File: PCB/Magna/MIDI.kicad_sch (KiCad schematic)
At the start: 14 parts, among them J1001 DIN-5_180degree, J1002 DIN-5_180degree, J1003 DIN-5_180degree, U1001 74HC08D, U1002 6N137

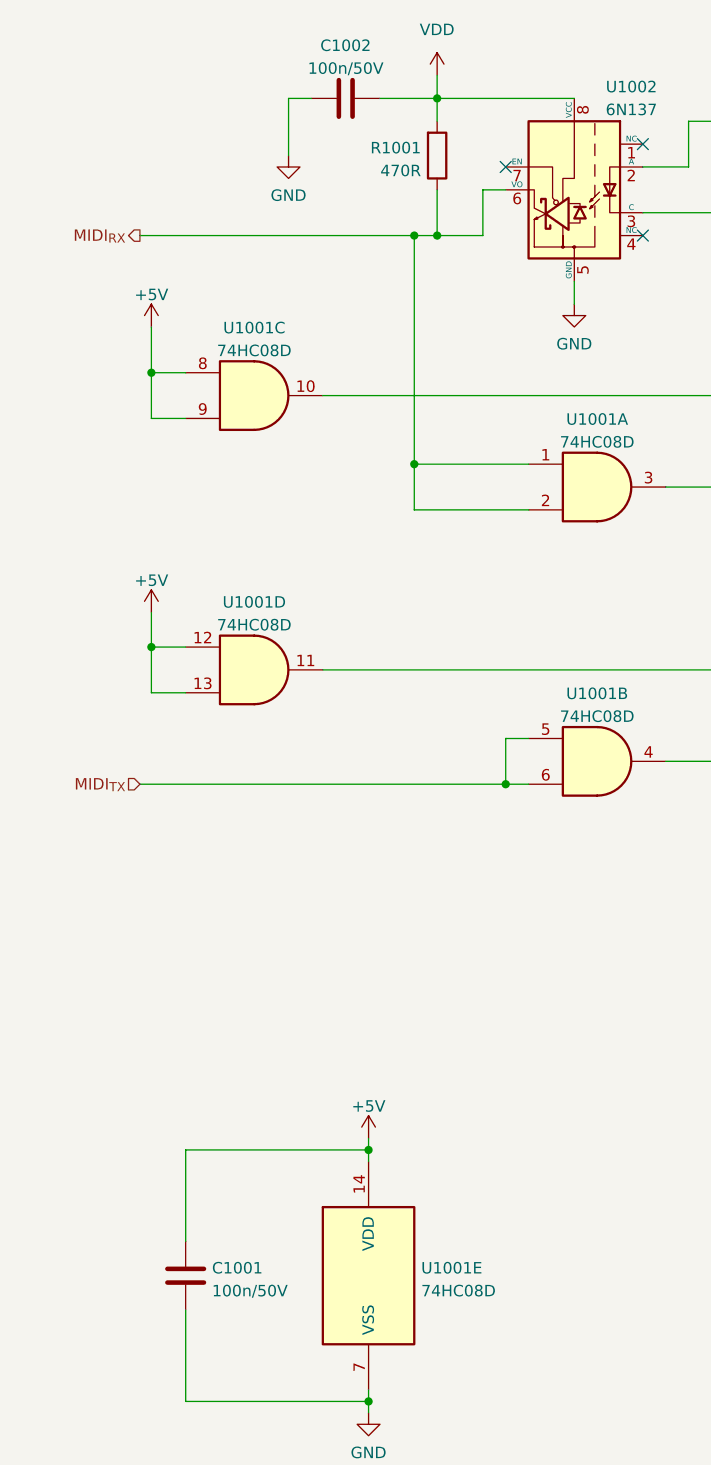
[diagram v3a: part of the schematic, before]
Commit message: Update capacitors to parts in JLC library
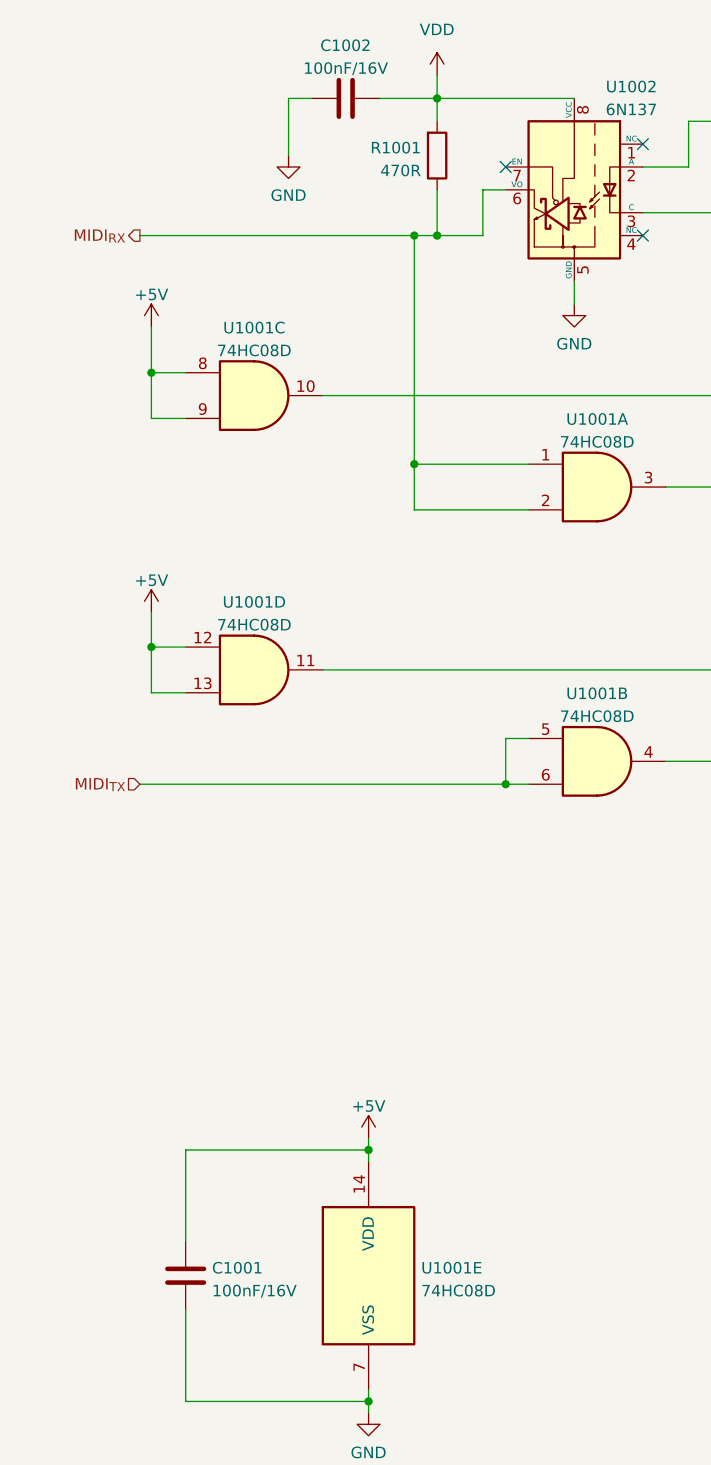
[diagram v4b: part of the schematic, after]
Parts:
- C1001, C1002: value 100n/50V -> 100nF/16V; footprint Capacitor_SMD:C_0603_1608Metric_Pad1.08x0.95mm_HandSolder -> Capacitor_SMD:C_0805_2012Metric; LCSC C14663 -> C218638
- D1001: LCSC C8598 -> (none)
- R1001: LCSC C23179 -> (none)
- R1002, R1003, R1004, R1005, R1006: LCSC C17557 -> (none)
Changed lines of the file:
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@@
       (effects (font (size 1.27 1.27)) hide)
     )
-    (property "LCSC" "C17557" (at 196.85 91.44 0)
+    (property "LCSC" "" (at 196.85 91.44 0)
       (effects (font (size 1.27 1.27)) hide)
     )
@@
       (effects (font (size 1.27 1.27)) (justify left))
     )
-    (property "Value" "100n/50V" (at 46.101 160.4522 0)
+    (property "Value" "100nF/16V" (at 46.101 160.4522 0)
       (effects (font (size 1.27 1.27)) (justify left))
     )
-    (property "Footprint" "Capacitor_SMD:C_0603_1608Metric_Pad1.08x0.95mm_HandSolder" (at 44.1452 162.56 0)
+    (property "Footprint" "Capacitor_SMD:C_0805_2012Metric" (at 44.1452 162.56 0)
       (effects (font (size 1.27 1.27)) hide)
     )
@@
       (effects (font (size 1.27 1.27)) hide)
     )
-    (property "LCSC" "C14663" (at 43.18 158.75 0)
+    (property "LCSC" "C218638" (at 43.18 158.75 0)
       (effects (font (size 1.27 1.27)) hide)
     )
@@
       (effects (font (size 1.27 1.27)) hide)
     )
-    (property "LCSC" "C17557" (at 196.85 101.6 0)
+    (property "LCSC" "" (at 196.85 101.6 0)
       (effects (font (size 1.27 1.27)) hide)
     )
@@
       (effects (font (size 1.27 1.27)) hide)
     )
-    (property "LCSC" "C17557" (at 196.85 43.18 0)
+    (property "LCSC" "" (at 196.85 43.18 0)
       (effects (font (size 1.27 1.27)) hide)
     )
@@
       (effects (font (size 1.27 1.27)) hide)
     )
-    (property "LCSC" "C17557" (at 196.85 60.96 0)
+    (property "LCSC" "" (at 196.85 60.96 0)
       (effects (font (size 1.27 1.27)) hide)
     )
@@
       (effects (font (size 1.27 1.27)))
     )
-    (property "Value" "100n/50V" (at 60.96 24.6181 90)
-      (effects (font (size 1.27 1.27)))
-    )
-    (property "Footprint" "Capacitor_SMD:C_0603_1608Metric_Pad1.08x0.95mm_HandSolder" (at 64.77 26.9748 0)
+    (property "Value" "100nF/16V" (at 60.96 24.6181 90)
+      (effects (font (size 1.27 1.27)))
+    )
+    (property "Footprint" "Capacitor_SMD:C_0805_2012Metric" (at 64.77 26.9748 0)
       (effects (font (size 1.27 1.27)) hide)
     )
@@
       (effects (font (size 1.27 1.27)) hide)
     )
-    (property "LCSC" "C14663" (at 60.96 27.94 0)
+    (property "LCSC" "C218638" (at 60.96 27.94 0)
       (effects (font (size 1.27 1.27)) hide)
     )
@@
       (effects (font (size 1.27 1.27)) hide)
     )
-    (property "LCSC" "C8598" (at 208.28 36.83 0)
+    (property "LCSC" "" (at 208.28 36.83 0)
       (effects (font (size 1.27 1.27)) hide)
     )
@@
       (effects (font (size 1.27 1.27)) hide)
     )
-    (property "LCSC" "C23179" (at 71.12 34.29 0)
+    (property "LCSC" "" (at 71.12 34.29 0)
       (effects (font (size 1.27 1.27)) hide)
     )
@@
       (effects (font (size 1.27 1.27)) hide)
     )
-    (property "LCSC" "C17557" (at 196.85 71.12 0)
-      (effects (font (size 1.27 1.27)) hide)
-    )
+    (property "LCSC" "" (at 196.85 71.12 0)
+      (effects (font (size 1.27 1.27)) hide)
+    )

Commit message: Select parts for all components
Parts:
- D1001: LCSC (none) -> C64885
- R1001: footprint Resistor_SMD:R_0603_1608Metric_Pad0.98x0.95mm_HandSolder -> Resistor_SMD:R_0805_2012Metric_Pad1.20x1.40mm_HandSolder; LCSC (none) -> C706320
- R1002, R1003, R1004, R1005, R1006: LCSC (none) -> C17557
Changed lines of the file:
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@@
       (effects (font (size 1.27 1.27)) hide)
     )
-    (property "LCSC" "" (at 196.85 91.44 0)
+    (property "LCSC" "C17557" (at 196.85 91.44 0)
       (effects (font (size 1.27 1.27)) hide)
     )
@@
       (effects (font (size 1.27 1.27)) hide)
     )
-    (property "LCSC" "" (at 196.85 101.6 0)
+    (property "LCSC" "C17557" (at 196.85 101.6 0)
       (effects (font (size 1.27 1.27)) hide)
     )
@@
       (effects (font (size 1.27 1.27)) hide)
     )
-    (property "LCSC" "" (at 196.85 43.18 0)
+    (property "LCSC" "C17557" (at 196.85 43.18 0)
       (effects (font (size 1.27 1.27)) hide)
     )
@@
       (effects (font (size 1.27 1.27)) hide)
     )
-    (property "LCSC" "" (at 196.85 60.96 0)
+    (property "LCSC" "C17557" (at 196.85 60.96 0)
       (effects (font (size 1.27 1.27)) hide)
     )
@@
       (effects (font (size 1.27 1.27)) hide)
     )
-    (property "LCSC" "" (at 208.28 36.83 0)
+    (property "LCSC" "C64885" (at 208.28 36.83 0)
       (effects (font (size 1.27 1.27)) hide)
     )
@@
       (effects (font (size 1.27 1.27)) (justify right))
     )
-    (property "Footprint" "Resistor_SMD:R_0603_1608Metric_Pad0.98x0.95mm_HandSolder" (at 69.342 34.29 90)
+    (property "Footprint" "Resistor_SMD:R_0805_2012Metric_Pad1.20x1.40mm_HandSolder" (at 69.342 34.29 90)
       (effects (font (size 1.27 1.27)) hide)
     )
@@
       (effects (font (size 1.27 1.27)) hide)
     )
-    (property "LCSC" "" (at 71.12 34.29 0)
+    (property "LCSC" "C706320" (at 71.12 34.29 0)
       (effects (font (size 1.27 1.27)) hide)
     )
@@
       (effects (font (size 1.27 1.27)) hide)
     )
-    (property "LCSC" "" (at 196.85 71.12 0)
-      (effects (font (size 1.27 1.27)) hide)
-    )
+    (property "LCSC" "C17557" (at 196.85 71.12 0)
+      (effects (font (size 1.27 1.27)) hide)
+    )

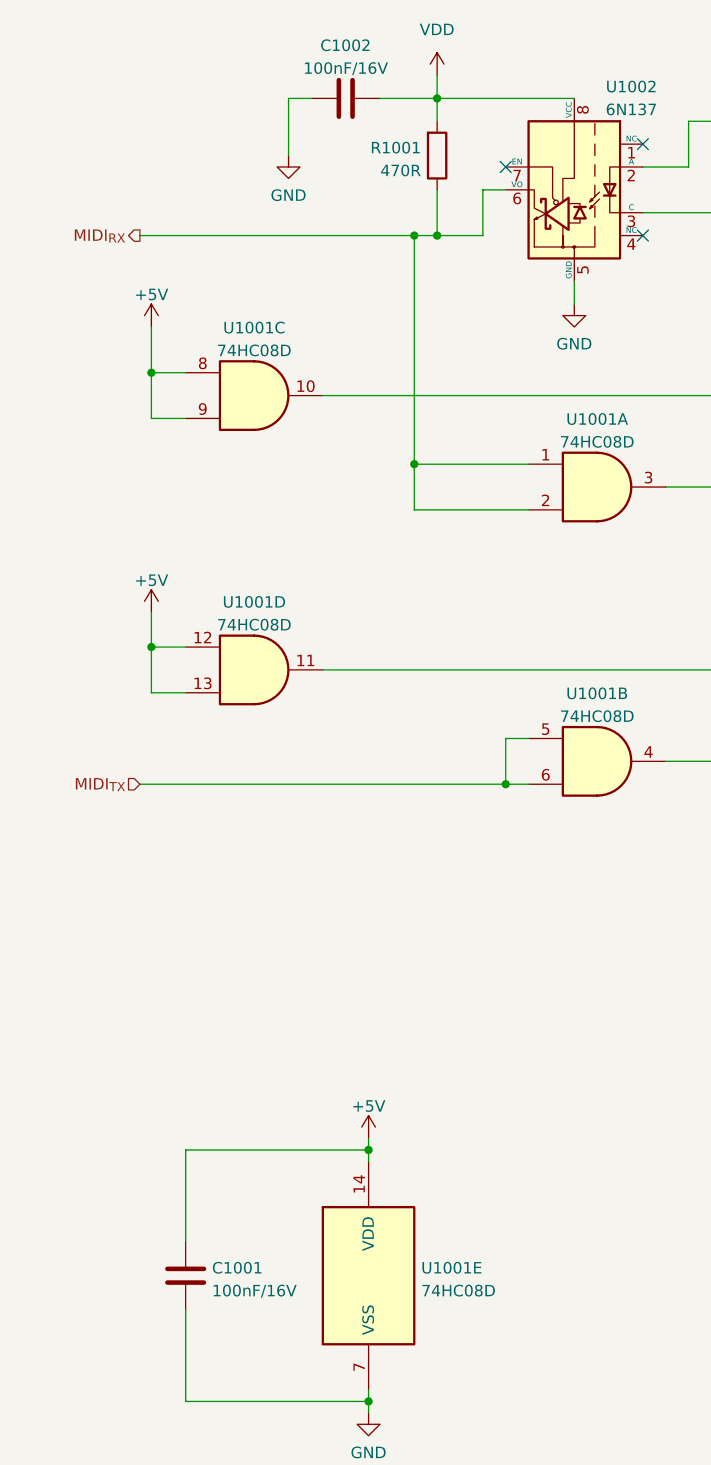
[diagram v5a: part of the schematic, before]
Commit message: Add even more component footprints and partnumbers
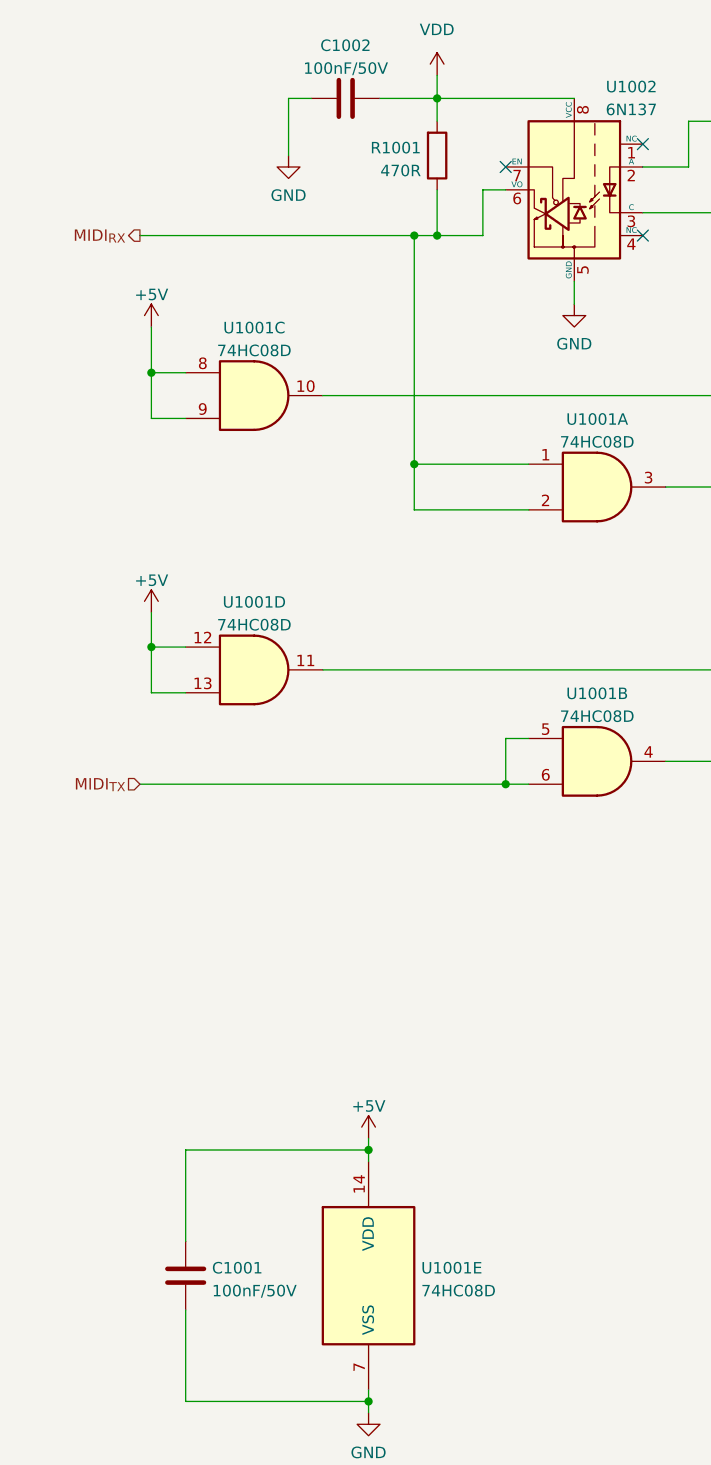
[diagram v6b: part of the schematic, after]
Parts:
- C1001, C1002: value 100nF/16V -> 100nF/50V; footprint Capacitor_SMD:C_0805_2012Metric -> Capacitor_SMD:C_0805_2012Metric_Pad1.18x1.45mm_HandSolder; LCSC C218638 -> C49678
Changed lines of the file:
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@@
       (effects (font (size 1.27 1.27)) (justify left))
     )
-    (property "Value" "100nF/16V" (at 46.101 160.4522 0)
+    (property "Value" "100nF/50V" (at 46.101 160.4522 0)
       (effects (font (size 1.27 1.27)) (justify left))
     )
-    (property "Footprint" "Capacitor_SMD:C_0805_2012Metric" (at 44.1452 162.56 0)
+    (property "Footprint" "Capacitor_SMD:C_0805_2012Metric_Pad1.18x1.45mm_HandSolder" (at 44.1452 162.56 0)
       (effects (font (size 1.27 1.27)) hide)
     )
@@
       (effects (font (size 1.27 1.27)) hide)
     )
-    (property "LCSC" "C218638" (at 43.18 158.75 0)
+    (property "LCSC" "C49678" (at 43.18 158.75 0)
       (effects (font (size 1.27 1.27)) hide)
     )
@@
       (effects (font (size 1.27 1.27)))
     )
-    (property "Value" "100nF/16V" (at 60.96 24.6181 90)
-      (effects (font (size 1.27 1.27)))
-    )
-    (property "Footprint" "Capacitor_SMD:C_0805_2012Metric" (at 64.77 26.9748 0)
+    (property "Value" "100nF/50V" (at 60.96 24.6181 90)
+      (effects (font (size 1.27 1.27)))
+    )
+    (property "Footprint" "Capacitor_SMD:C_0805_2012Metric_Pad1.18x1.45mm_HandSolder" (at 64.77 26.9748 0)
       (effects (font (size 1.27 1.27)) hide)
     )
@@
       (effects (font (size 1.27 1.27)) hide)
     )
-    (property "LCSC" "C218638" (at 60.96 27.94 0)
-      (effects (font (size 1.27 1.27)) hide)
-    )
+    (property "LCSC" "C49678" (at 60.96 27.94 0)
+      (effects (font (size 1.27 1.27)) hide)
+    )
